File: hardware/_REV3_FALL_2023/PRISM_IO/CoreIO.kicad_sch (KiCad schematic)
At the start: 30 parts, among them J2 COTS_SWITCH_PLUG, J3 PYRO 1, J4 PYRO 2, Q1 AO3400A, Q2 AO3400A

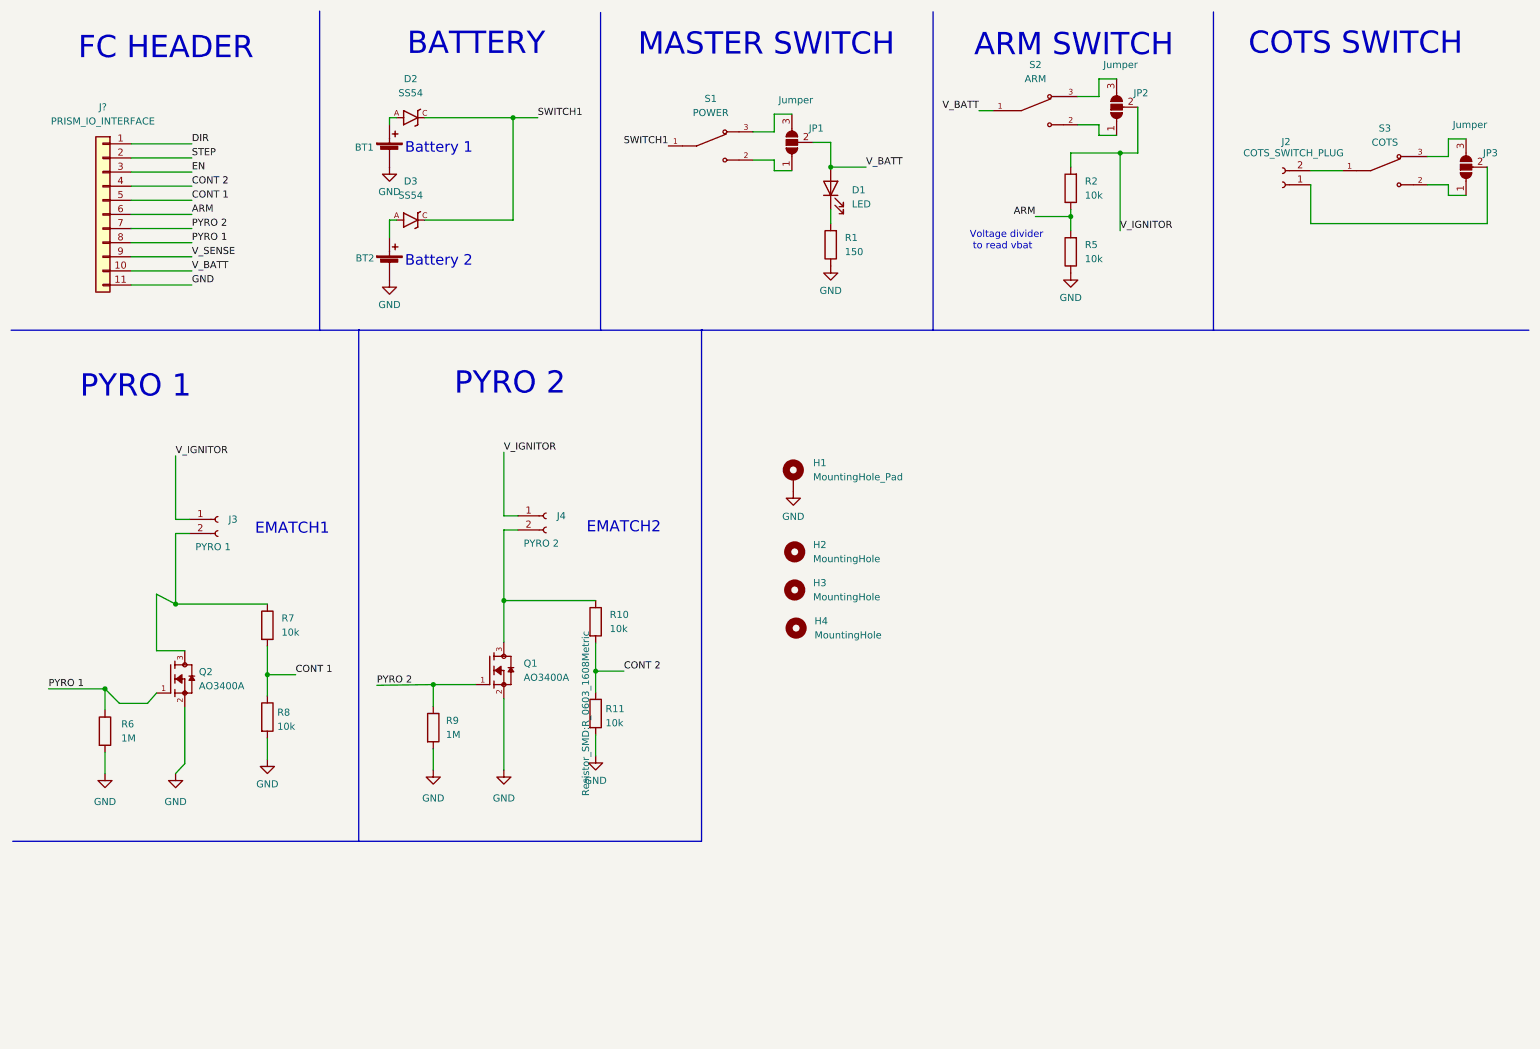
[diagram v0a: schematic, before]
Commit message: update Core IO schematic and first layout concept
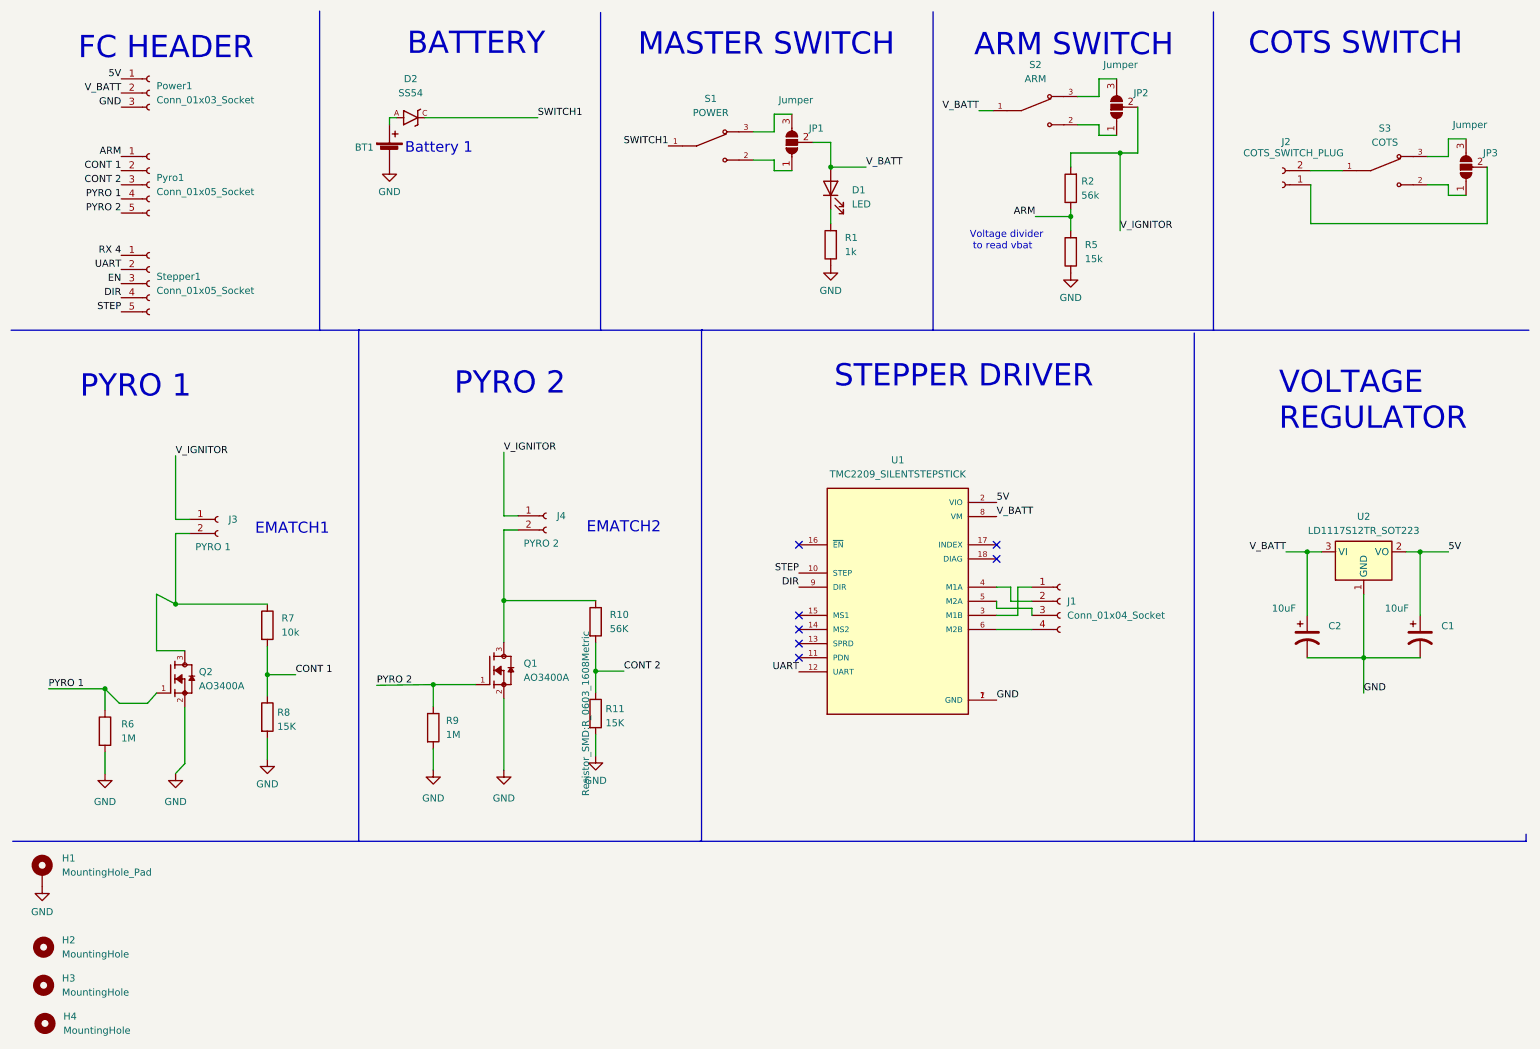
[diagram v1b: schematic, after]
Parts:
- removed BT2: ~, JST:JST_SFH_SM02B-SFHRS-TF_02x1.80mm_Angled, symbol Device:Battery_Cell
- removed D3: SS54, JLC_footprints:DO-214AC, symbol SS54:SS54
- removed J?: PRISM_IO_INTERFACE, symbol Connector_Generic:Conn_01x11
- added C1, C2: 10uF, Capacitor_SMD:CP_Elec_4x5.4, symbol Device:C_Polarized_US
- added J1: Conn_01x04_Socket, Connectors_JST.pretty-master:JST_XH_S04B-XH-A_04x2.50mm_Angled, symbol Connector:Conn_01x04_Socket
- added Power1: Conn_01x03_Socket, Connector_PinHeader_2.54mm:PinHeader_1x03_P2.54mm_Vertical, symbol Connector:Conn_01x03_Socket
- added Pyro1, Stepper1: Conn_01x05_Socket, Connector_PinHeader_2.54mm:PinHeader_1x05_P2.54mm_Vertical, symbol Connector:Conn_01x05_Socket
- added U1: TMC2209_SILENTSTEPSTICK, TMC2209_SILENTSTEPSTICK:MODULE_TMC2209_SILENTSTEPSTICK, symbol TMC2209_SILENTSTEPSTICK:TMC2209_SILENTSTEPSTICK
- added U2: LD1117S12TR_SOT223, Package_TO_SOT_SMD:SOT-223-3_TabPin2, symbol Regulator_Linear:LD1117S12TR_SOT223
- BT1, J3, J4: footprint JST:JST_SFH_SM02B-SFHRS-TF_02x1.80mm_Angled -> Connectors_JST.pretty-master:JST_XH_S02B-XH-A_02x2.50mm_Angled
- J2: footprint Connector_JST:JST_PH_S2B-PH-K_1x02_P2.00mm_Horizontal -> Connectors_JST.pretty-master:JST_XH_S02B-XH-A_02x2.50mm_Angled
- R1: value 150 -> 1k; Vendor C22808 -> C21190
- R10: value 10k -> 56K; Vendor C25804 -> C23206
- R11, R8: value 10k -> 15K; Vendor C25804 -> C22809
- R2: value 10k -> 56k; Vendor C25804 -> C23206
- R5: value 10k -> 15k; Vendor C25804 -> C22809
- R7: Vendor C25804 -> C23206
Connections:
- net ARM: now also Pyro1.1 (Pin_1)
- net CONT 1: now also Pyro1.2 (Pin_2)
- net CONT 2: now also Pyro1.3 (Pin_3)
- net DIR: now also Stepper1.4 (Pin_4), U1.9 (DIR)
- net EN: now also Stepper1.3 (Pin_3)
- net GND: now also C1.2, C2.2, Power1.3 (Pin_3), U1.1 (GND), U1.7 (GND), U2.1 (GND)
- net PYRO 1: now also Pyro1.4 (Pin_4)
- net PYRO 2: now also Pyro1.5 (Pin_5)
- net STEP: now also Stepper1.5 (Pin_5), U1.10 (STEP)
- net V_BATT: now also C2.1, Power1.2 (Pin_2), U1.8 (VM), U2.3 (VI)
- new net: J1.1 (Pin_1), U1.3 (M1B)
- new net: J1.2 (Pin_2), U1.4 (M1A)
- new net: J1.3 (Pin_3), U1.5 (M2A)
- new net: J1.4 (Pin_4), U1.6 (M2B)
- new net 5V: C1.1, Power1.1 (Pin_1), U1.2 (VIO), U2.2 (VO)
- new net RX 4: Stepper1.1 (Pin_1)
- new net UART: Stepper1.2 (Pin_2), U1.12 (UART)
- no-connect marks 0 -> 7
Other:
- note added: "STEPPER DRIVER"
- note added: "VOLTAGE REGULATOR"
- note removed: "Battery 2"
- moved on the sheet: H1, H2, H3, H4

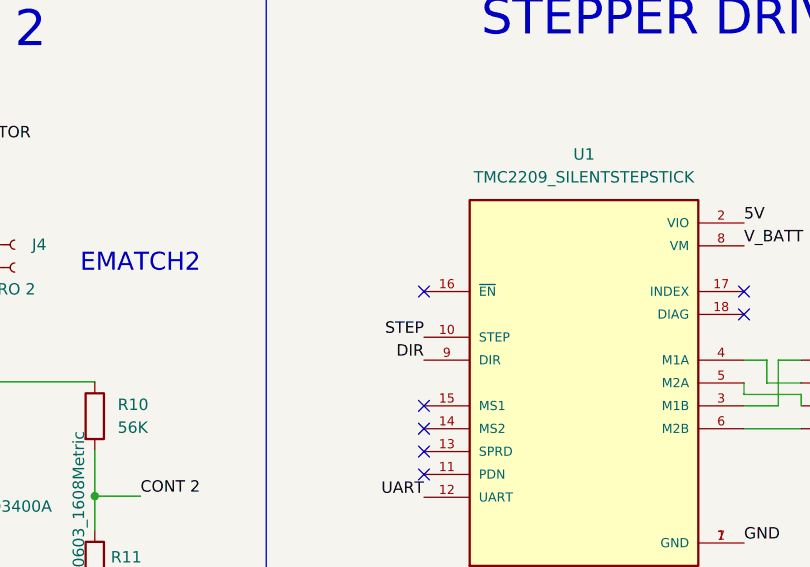
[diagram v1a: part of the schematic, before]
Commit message: fixed stepper wiring
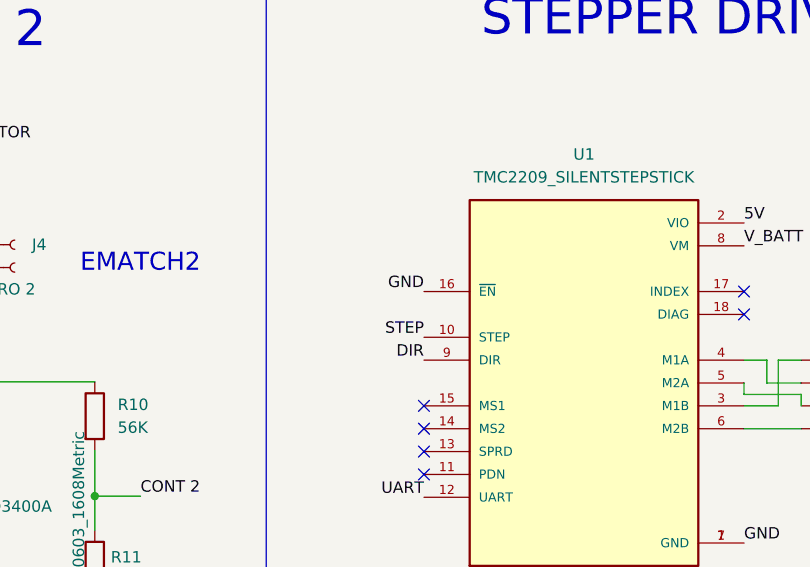
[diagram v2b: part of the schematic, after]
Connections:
- net GND: now also U1.16 (~{EN})
- no-connect marks 7 -> 6
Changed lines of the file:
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@@
   (junction (at 211.455 37.465) (diameter 0) (color 0 0 0 0)
   )
+  (no_connect (at 153.67 123.19))
   (no_connect (at 153.67 128.27))
-  (no_connect (at 153.67 107.95))
-  (no_connect (at 153.67 123.19))
   (no_connect (at 153.67 120.65))
   (no_connect (at 189.23 110.49))
+  (no_connect (at 189.23 107.95))
   (no_connect (at 153.67 125.73))
-  (no_connect (at 189.23 107.95))
   (wire (pts (xy 117.094 142.113) (xy 117.094 145.923))
     (stroke (width 0) (type default))
@@
     (effects (font (size 1.27 1.27)) (justify left bottom))
   )
+  (label "GND" (at 153.67 107.95 180) (fields_autoplaced)
+    (effects (font (size 1.27 1.27)) (justify right bottom))
+  )
   (label "PYRO 1" (at 31.75 45.72 180) (fields_autoplaced)

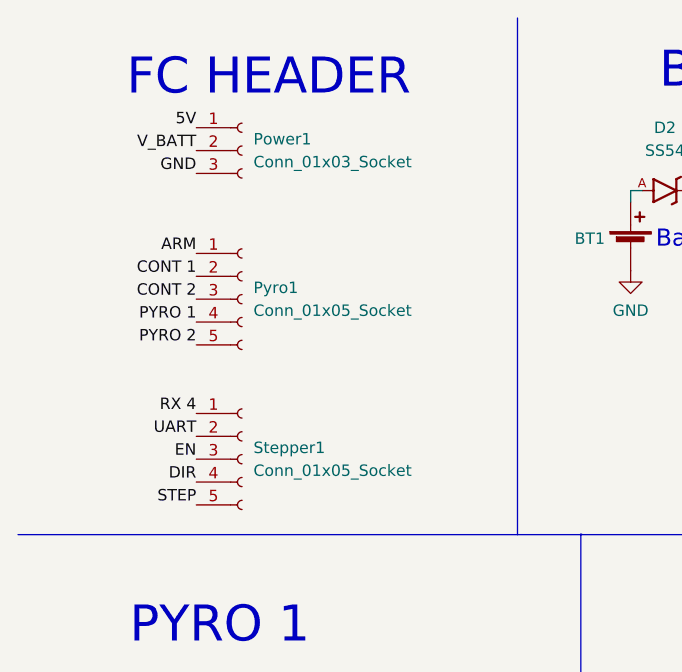
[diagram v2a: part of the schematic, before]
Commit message: finished IO layout
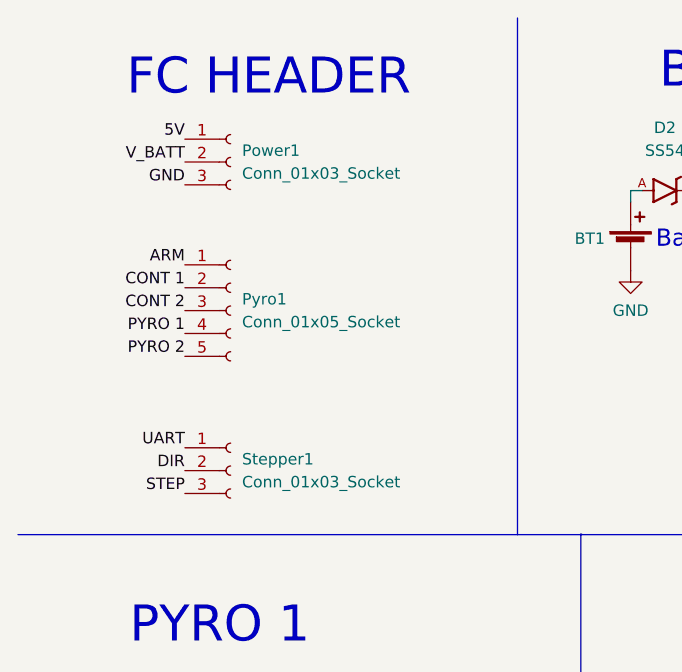
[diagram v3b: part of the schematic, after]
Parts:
- removed Stepper1: Conn_01x05_Socket, Connector_PinHeader_2.54mm:PinHeader_1x05_P2.54mm_Vertical, symbol Connector:Conn_01x05_Socket
- added Stepper1: Conn_01x03_Socket, Connector_PinHeader_2.54mm:PinHeader_1x03_P2.54mm_Vertical, symbol Connector:Conn_01x03_Socket
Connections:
- net DIR: now also Stepper1.2 (Pin_2)
- net STEP: now also Stepper1.3 (Pin_3)
- net UART: now also Stepper1.1 (Pin_1)

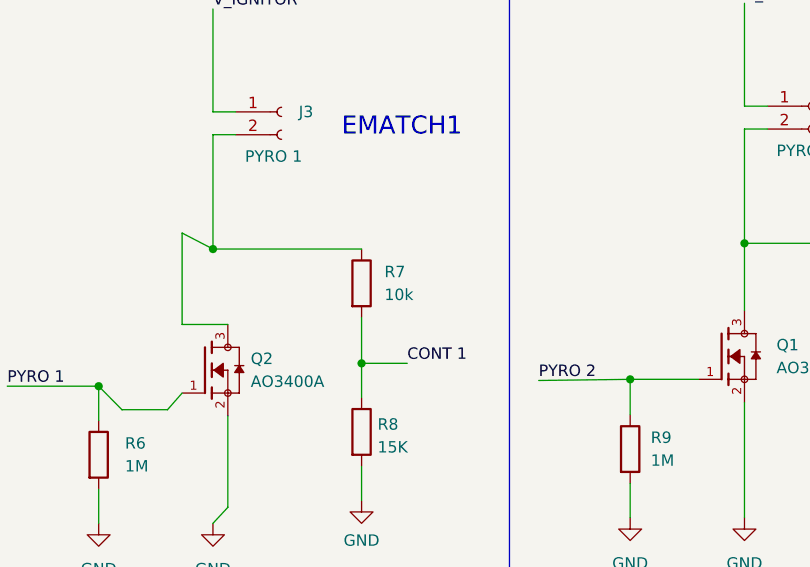
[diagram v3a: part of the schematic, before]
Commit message: Add aesthetics to IO board
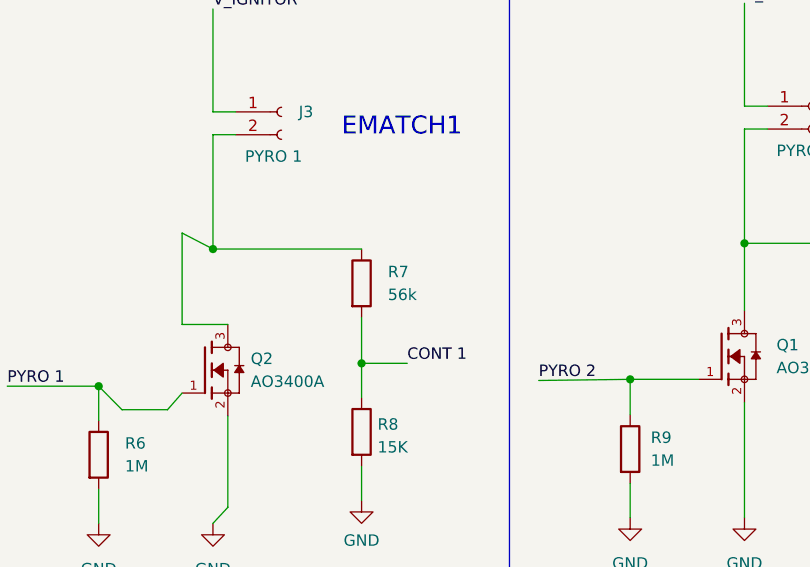
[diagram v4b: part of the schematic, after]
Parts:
- R7: value 10k -> 56k
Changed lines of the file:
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@@
       (effects (font (size 1.27 1.27)) (justify bottom) hide)
     )
+    (pin "1")
+    (pin "10")
+    (pin "11")
+    (pin "12")
+    (pin "13")
+    (pin "14")
     (pin "15")
+    (pin "16")
+    (pin "17")
+    (pin "18")
+    (pin "2")
+    (pin "3")
+    (pin "4")
+    (pin "5")
+    (pin "6")
     (pin "7")
-    (pin "14")
     (pin "8")
-    (pin "10")
     (pin "9")
-    (pin "13")
-    (pin "17")
-    (pin "11")
-    (pin "1")
-    (pin "5")
-    (pin "16")
-    (pin "3")
-    (pin "18")
-    (pin "4")
-    (pin "2")
-    (pin "12")
-    (pin "6")
     (instances
       (project "CoreIO"
@@
     )
     (pin "1")
-    (pin "3")
-    (pin "2")
+    (pin "2")
+    (pin "3")
     (instances
       (project "CoreIO"
@@
   (symbol (lib_id "Device:R") (at 58.039 122.428 0) (unit 1)
     (in_bom yes) (on_board yes) (dnp no) (fields_autoplaced)
-    (property "Reference" "R7" (at 60.579 121.1579 0)
-      (effects (font (size 1.27 1.27)) (justify left))
-    )
-    (property "Value" "10k" (at 60.579 123.6979 0)
+    (property "Reference" "R7" (at 60.96 121.158 0)
+      (effects (font (size 1.27 1.27)) (justify left))
+    )
+    (property "Value" "56k" (at 60.96 123.698 0)
       (effects (font (size 1.27 1.27)) (justify left))
     )
@@
       (effects (font (size 1.27 1.27)) hide)
     )
-    (pin "3")
-    (pin "2")
-    (pin "1")
+    (pin "1")
+    (pin "2")
+    (pin "3")
     (pin "4")
     (instances

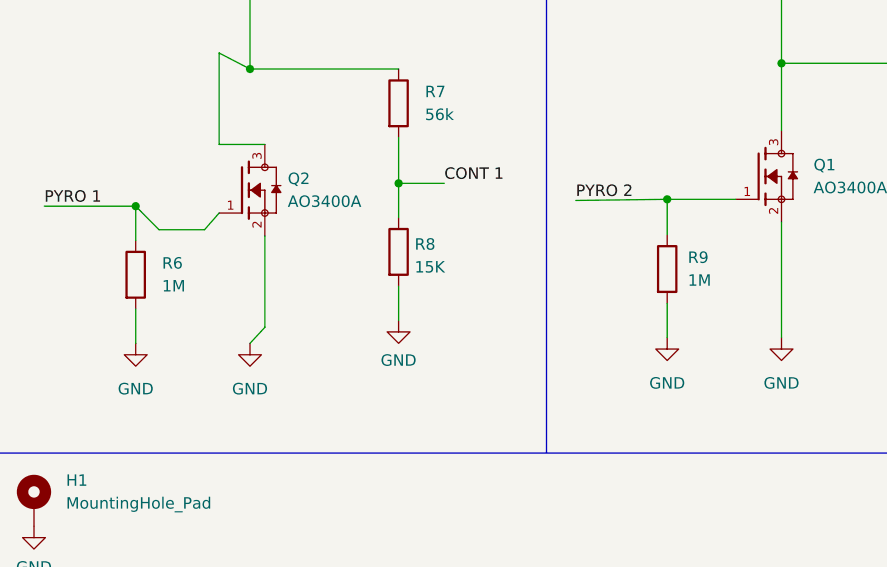
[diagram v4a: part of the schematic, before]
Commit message: Change IO pulldown resistors
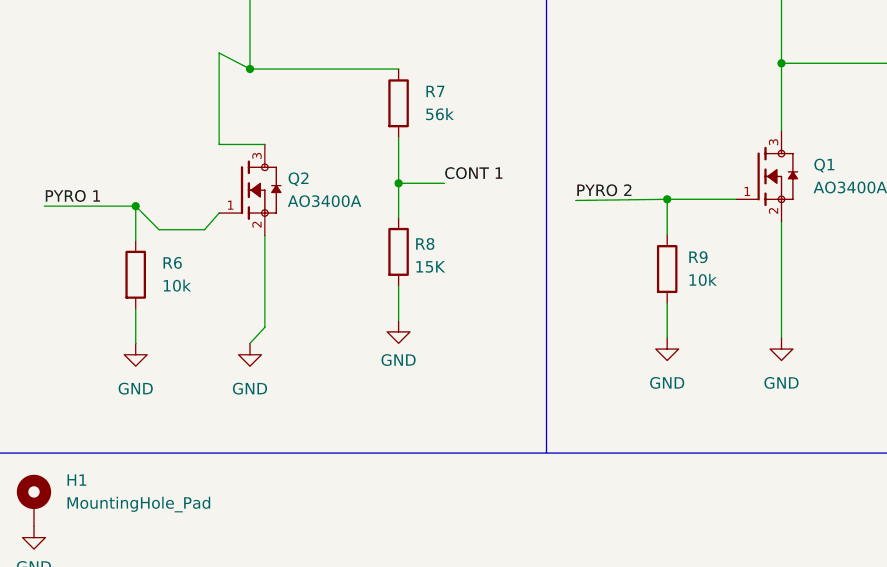
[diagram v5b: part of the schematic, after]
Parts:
- R6, R9: value 1M -> 10k; Vendor C22935 -> C25804
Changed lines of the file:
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@@
       (effects (font (size 1.27 1.27)) (justify left))
     )
-    (property "Value" "1M" (at 90.17 142.1129 0)
+    (property "Value" "10k" (at 90.17 142.1129 0)
       (effects (font (size 1.27 1.27)) (justify left))
     )
@@
       (effects (font (size 1.27 1.27)) hide)
     )
-    (property "Vendor" "C22935" (at 87.884 140.843 0)
+    (property "Vendor" "C25804" (at 87.884 140.843 0)
       (effects (font (size 1.27 1.27)) hide)
     )
@@
       (effects (font (size 1.27 1.27)) (justify left))
     )
-    (property "Value" "1M" (at 31.75 142.7479 0)
+    (property "Value" "10k" (at 31.75 142.7479 0)
       (effects (font (size 1.27 1.27)) (justify left))
     )
@@
       (effects (font (size 1.27 1.27)) hide)
     )
-    (property "Vendor" "C22935" (at 28.829 141.478 0)
-      (effects (font (size 1.27 1.27)) hide)
-    )
+    (property "Vendor" "C25804" (at 28.829 141.478 0)
+      (effects (font (size 1.27 1.27)) hide)
+    )
